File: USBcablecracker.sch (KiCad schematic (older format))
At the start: 51 parts, among them IC1 ATTINY85-S, P1 USB_A_L, P10 USB_A_R, P11 USB_B_R, P12 CONN_01X06, P2 USB_B_L, P3 USB_TYPEC-S, P4 USB_MINI_L, P5 USB_MICRO_L, P6 USB_OTG, P7 USB_MINI_R, P8 USB_MICRO_R, P9 USB_TYPEC-S, Q1 S8050, SW1 Switch_SPDT_x2, U1 PCF8574, U2 LMV358, U3 AD623

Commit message: ATtiny85>>Atmega32u4
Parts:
- removed C1, C6: 0.1uF, Capacitors_SMD:C_0603_HandSoldering, symbol C_Small
- removed C5: 4.7uF, Capacitors_SMD:C_0603_HandSoldering, symbol C_Small
- removed D1: S4, AirBox:SOD-323, symbol D_Small
- removed D2, D3: W4, AirBox:SOD-323, symbol D_Schottky_Small
- removed D5: BLUE, LEDs:LED_0603, symbol Led_Small
- removed D6: RED, LEDs:LED_0603, symbol Led_Small
- removed DS1: LCD16X2, Display:WC1602A, symbol LCD16X2
- removed IC1: ATTINY85-S, Housings_SOIC:SOIJ-8_5.3x5.3mm_Pitch1.27mm, symbol ATTINY85-S
- removed P12: CONN_01X06, SmartEye:TestPin_Header_Straight_1x06, symbol CONN_01X06
- removed P6: USB_OTG, SmartEye:USB_Micro-B, symbol USB_OTG
- removed Q1: S8050, TO_SOT_Packages_SMD:SOT-23_Handsoldering, symbol S8050
- removed R1, R2, R3, R5, R6: 10K, Resistors_SMD:R_0603_HandSoldering, symbol R_Small
- removed R20: 470R, Resistors_SMD:R_0603_HandSoldering, symbol R_Small
- removed R21, R4: 1K, Resistors_SMD:R_0603_HandSoldering, symbol R_Small
- removed R7: 1.5K, Resistors_SMD:R_0603_HandSoldering, symbol R_Small
- removed R8, R9: 68R, Resistors_SMD:R_0603_HandSoldering, symbol R_Small
- removed RV1: POT, USBcablecracker:BOURNS-3362P_pot, symbol POT
- removed U1: PCF8574, Housings_SOIC:SOIC-16W_7.5x10.3mm_Pitch1.27mm, symbol PCF8574
- added C? (x2): 100nF, Capacitors_ThroughHole:C_Rect_L7_W2_P5, symbol C_Small
- added C?: 1uF, Capacitors_ThroughHole:C_Rect_L7_W2_P5, symbol C_Small
- added C? (x2): 22P, Capacitors_ThroughHole:C_Rect_L7_W2_P5, symbol C_Small
- added C?: 22uF, Capacitors_ThroughHole:C_Radial_D5_L11_P2.5, symbol CP_Small
- added CONN?: ICSP, Connectors:CONN_2.54mm_2x3, symbol CONN_02X03
- added CONN?: USB_B, SmartEye:USB_Micro-B, symbol USB_B
- added D?: RX, LEDs:LED-5MM, symbol Led_Small
- added D?: TX, LEDs:LED-5MM, symbol Led_Small
- added D?: L, LEDs:LED-5MM, symbol Led_Small
- added D?: ON, LEDs:LED-5MM, symbol Led_Small
- added DS?: LCD16X2, Display:WC1602A, symbol LCD16X2
- added P? (x2): CONN_01X09, symbol CONN_01X09
- added R?: 91R, Resistors_SMD:R_0603_HandSoldering, symbol R_Small
- added R? (x2): 10K, Resistors_ThroughHole:Resistor_Horizontal_RM10mm, symbol R_Small
- added R? (x5): 1K, Resistors_ThroughHole:Resistor_Horizontal_RM10mm, symbol R_Small
- added R? (x2): 22R, Resistors_ThroughHole:Resistor_Horizontal_RM10mm, symbol R_Small
- added SW?: SW_RESET, Buttons_Switches_ThroughHole:SW_PUSH_6mm, symbol SW_PUSH
- added U?: ATmega32U4-AU, Housings_QFP:TQFP-44_10x10mm_Pitch0.8mm, symbol ATmega32U4-AU
- added Y?: 16MHz, Crystals:Crystal_HC49-U_Vertical, symbol Crystal_Small
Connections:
- net labels added: A0, A1, A2, A3, A4, A5, D+, D-, D0, D1, D2, D3, D4, D5, D6, D7, HWB, IO10, IO11, IO12, IO13, IO8, IO9, LED, MISO, MOSI, RESET, RX_LED, SCK, TX_LED, VBUS
- net labels removed: A, CS, DB4, DB5, DB6, DB7, K, P3, RS, RW, TO_ADC, VO
- wire segments 211 -> 257
- no-connect marks 24 -> 23
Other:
- moved on the sheet: C2, C3, C4, P1, P10, P11, P2, P3, P4, P5, P7, P8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

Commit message: update pcb
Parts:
- removed SW?: SW_RESET, Buttons_Switches_ThroughHole:SW_PUSH_6mm, symbol SW_PUSH
- C1, C5, C6, C7, C9: renamed from C?; footprint Capacitors_ThroughHole:C_Rect_L7_W2_P5 -> Capacitors_SMD:C_0603_HandSoldering
- C8: renamed from C?; footprint Capacitors_ThroughHole:C_Radial_D5_L11_P2.5 -> Capacitors_Tantalum_SMD:Tantalum_Case-A_EIA-3216-18_Wave
- CONN2: renamed from CONN?; symbol USB_B -> USB_B-RESCUE-USBcablecracker
- D1, D2, D3, D4: renamed from D?; footprint LEDs:LED-5MM -> LEDs:LED_0603
- P1, P10, P11, P2, P4, P7: symbol USB_A -> USB_A-RESCUE-USBcablecracker
- P12, P6: renamed from P?; footprint (none) -> Connectors:CONN_2.54mm_1x9
- P5, P8: symbol USB_OTG -> USB_OTG-RESCUE-USBcablecracker
- R1, R2, R3, R4, R5, R6, R7, R8, R9: renamed from R?; footprint Resistors_ThroughHole:Resistor_Horizontal_RM10mm -> Resistors_SMD:R_0603_HandSoldering
- R13: value 10K -> 100K
- R17: value 10K -> 100R
- U1: renamed from U?; symbol ATmega32U4-AU -> ATmega32U4-AU-RESCUE-USBcablecracker
- Y1: renamed from Y?; footprint Crystals:Crystal_HC49-U_Vertical -> Crystals:crystal_FA238-TSX3225
- gave numbers to parts that had none: 3
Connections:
- wire segments 257 -> 256

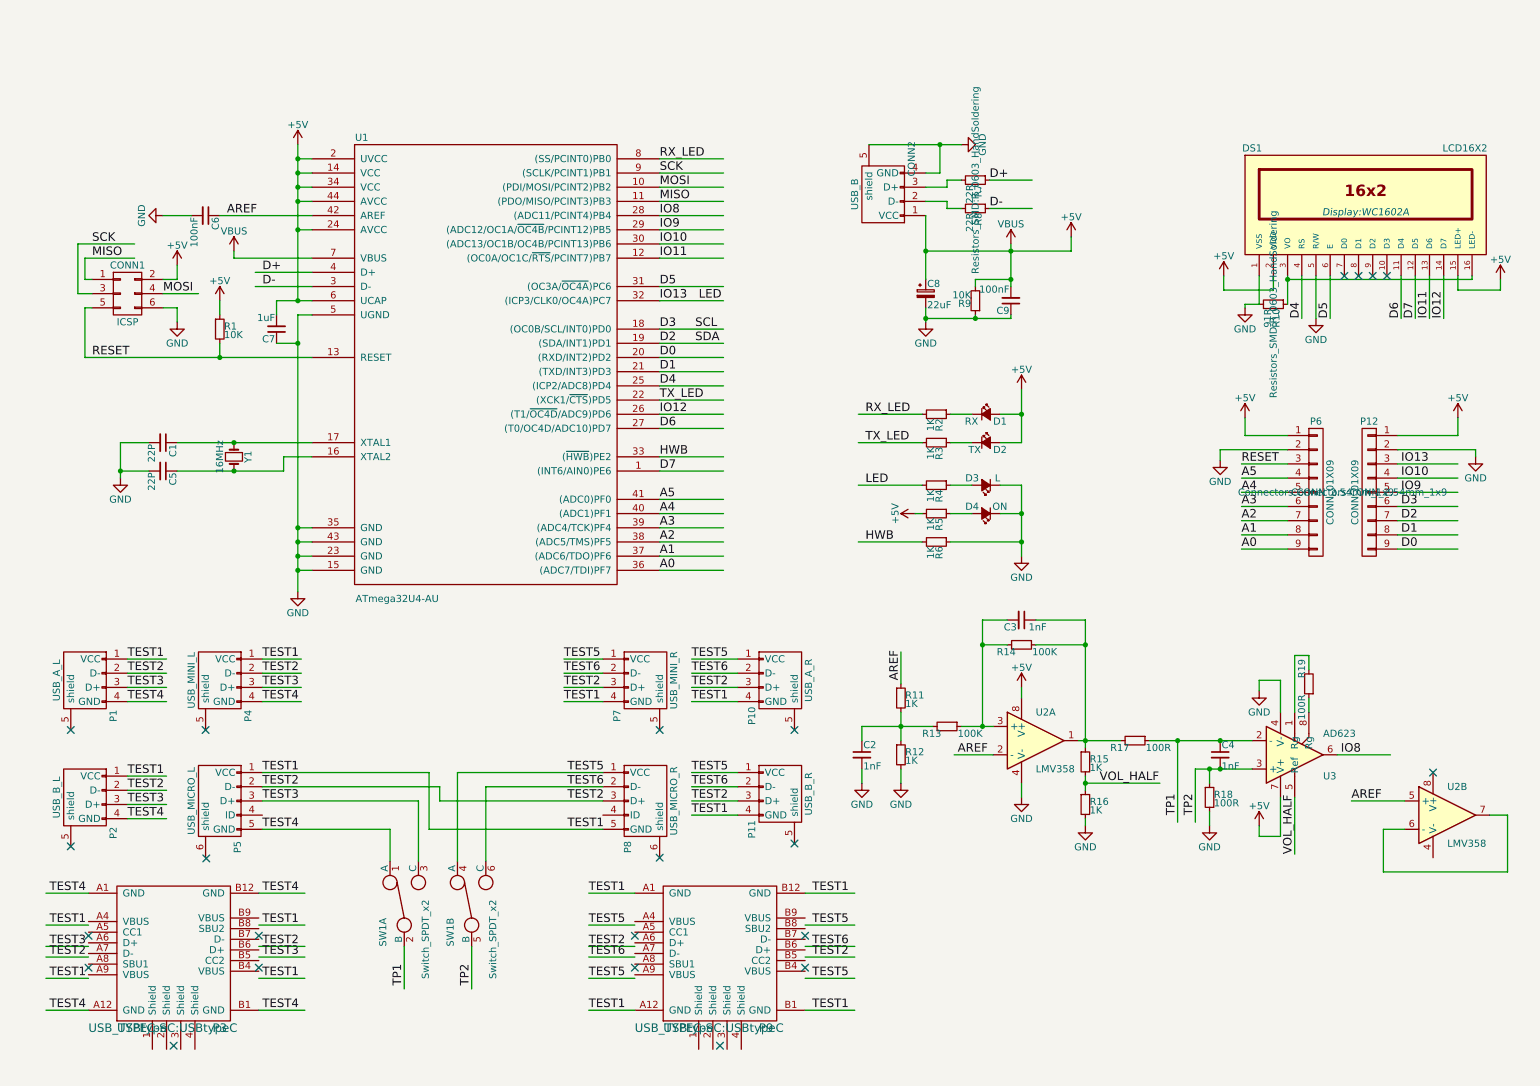
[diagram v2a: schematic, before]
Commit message: Version 0.4 finished. Solved UCAP inner linear regulator problem. Modified library, footprints, instrumentation amplifier common mode input voltage, modified AREF output load.
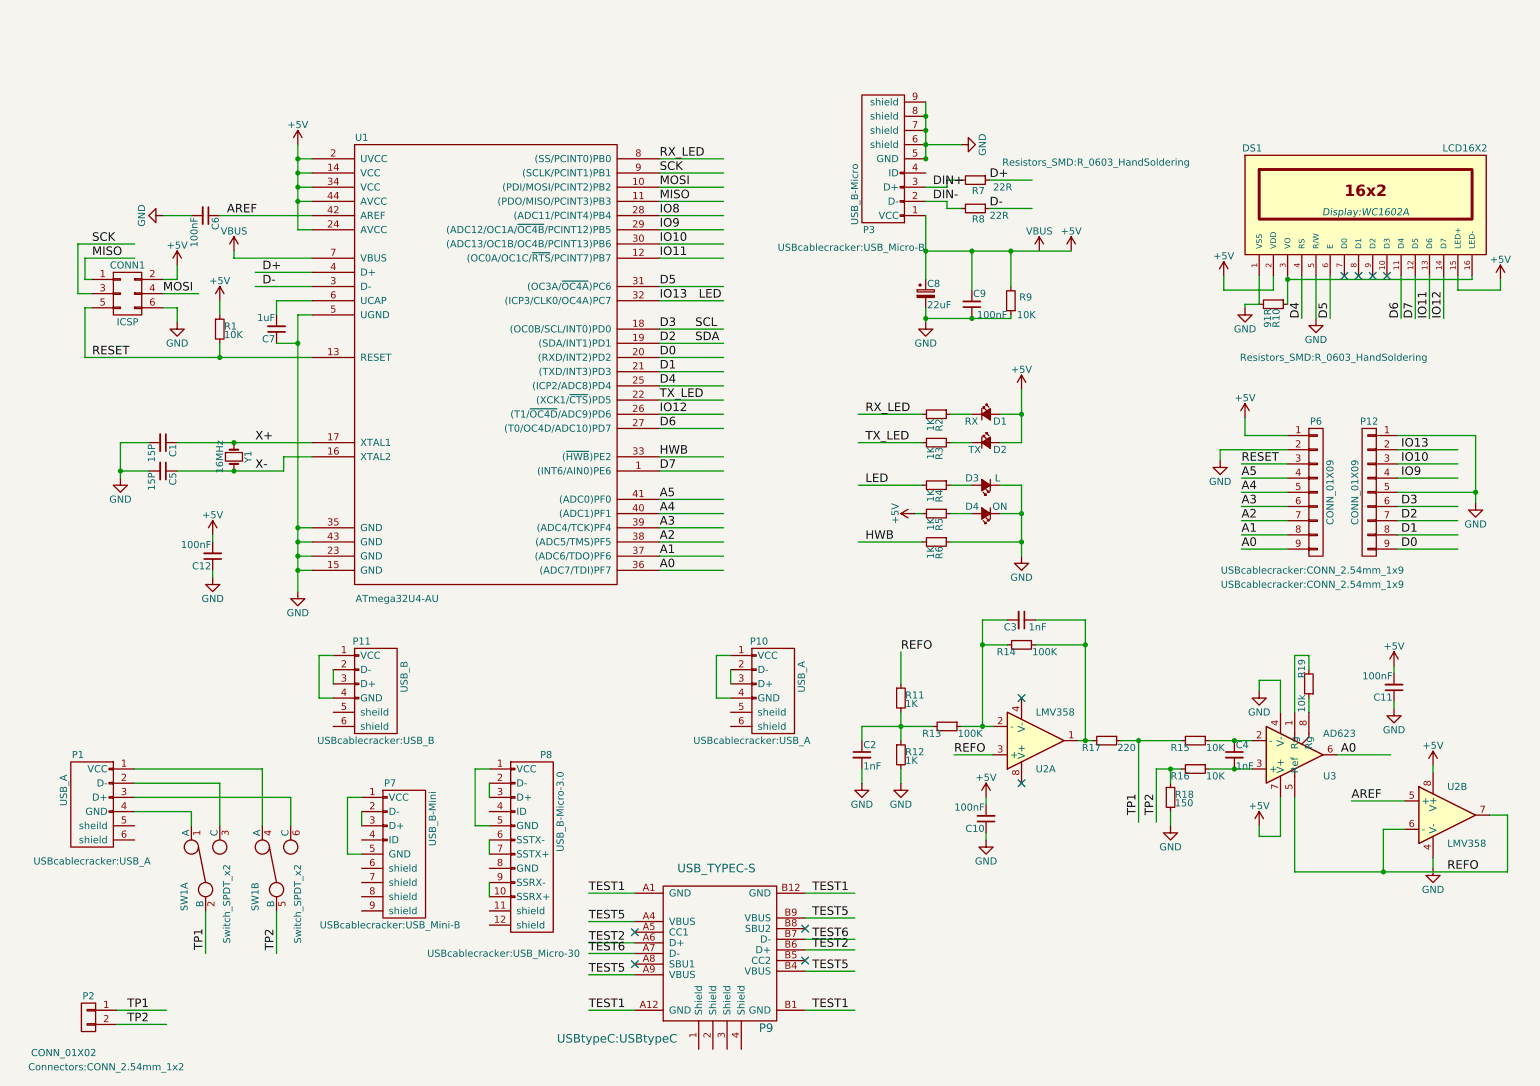
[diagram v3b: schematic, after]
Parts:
- removed CONN2: USB_B, SmartEye:USB_Micro-B, symbol USB_B-RESCUE-USBcablecracker
- removed P1: USB_A_L, Connect:USB_A, symbol USB_A-RESCUE-USBcablecracker
- removed P10: USB_A_R, Connect:USB_A, symbol USB_A-RESCUE-USBcablecracker
- removed P11: USB_B_R, Connect:USB_B, symbol USB_A-RESCUE-USBcablecracker
- removed P2: USB_B_L, Connect:USB_B, symbol USB_A-RESCUE-USBcablecracker
- removed P3: USB_TYPEC-S, USBtypeC:USBtypeC, symbol USB_TYPEC-S
- removed P4: USB_MINI_L, Connect:USB_Mini-B, symbol USB_A-RESCUE-USBcablecracker
- removed P5: USB_MICRO_L, SmartEye:USB_Micro-B, symbol USB_OTG-RESCUE-USBcablecracker
- removed P7: USB_MINI_R, Connect:USB_Mini-B, symbol USB_A-RESCUE-USBcablecracker
- removed P8: USB_MICRO_R, SmartEye:USB_Micro-B, symbol USB_OTG-RESCUE-USBcablecracker
- added C10, C11, C12: 100nF, Capacitors_SMD:C_0603_HandSoldering, symbol C_Small
- added P1, P10: USB_A, USBcablecracker:USB_A, symbol USB_A
- added P11: USB_B, USBcablecracker:USB_B, symbol USB_A
- added P2: CONN_01X02, Connectors:CONN_2.54mm_1x2, symbol CONN_01X02
- added P3: USB_B-Micro, USBcablecracker:USB_Micro-B, symbol USB_B-Micro
- added P7: USB_B-Mini, USBcablecracker:USB_Mini-B, symbol USB_B-Mini
- added P8: USB_B-Micro-3.0, USBcablecracker:USB_Micro-30, symbol USB_B-Micro-3.0
- C1, C5: value 22P -> 15P
- P12, P6: footprint Connectors:CONN_2.54mm_1x9 -> USBcablecracker:CONN_2.54mm_1x9
- R15, R16: value 1K -> 10K
- R17: value 100R -> 220
- R18: value 100R -> 150
- R19: value 100R -> 10k
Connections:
- net labels added: DIN+, DIN-, REFO, X+, X-
- net labels removed: TEST3, TEST4, VOL_HALF
- wire segments 256 -> 234
- no-connect marks 23 -> 10
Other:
- moved on the sheet: C4, C9, R17, R18, R9, SW1A, SW1B

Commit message: fangzhou
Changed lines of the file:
@@
 F 0 "P12" H 10000 4150 50  0000 C CNN
 F 1 "CONN_01X09" V 10100 3650 50  0000 C CNN
-F 2 "USBcablecracker:CONN_2.54mm_1x9" H 10400 3000 50  0000 C CNN
+F 2 "USBcablecracker:CONN_2.54mm_1x9" H 10325 3000 50  0000 C CNN
 F 3 "" H 10000 3650 50  0000 C CNN
 	1    10000 3650
@@
 F 0 "P6" H 9625 4150 50  0000 C CNN
 F 1 "CONN_01X09" V 9725 3650 50  0000 C CNN
-F 2 "USBcablecracker:CONN_2.54mm_1x9" H 9600 3100 50  0000 C CNN
+F 2 "USBcablecracker:CONN_2.54mm_1x9" H 9675 3100 50  0000 C CNN
 F 3 "" H 9625 3650 50  0000 C CNN
 	1    9625 3650

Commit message: update
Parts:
- added C13: 1nF, Capacitors_SMD:C_0603_HandSoldering, symbol C_Small
- added R20, R21, R22: 10K, Resistors_SMD:R_0603_HandSoldering, symbol R_Small
- R11: value 1K -> 10K
- R12: value 1K -> 100K
- R13: value 100K -> 10K
- R17: value 220 -> 68
- R18: value 150 -> 33
- R19: value 10k -> 11k
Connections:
- wire segments 234 -> 220
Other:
- note added: "Circuit in dashed lined rectangle has the same function.\nSelect one of them to solder."
- moved on the sheet: C10, C11, C2, C3, C4, C8, C9, D1, D2, D3, D4, DS1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
